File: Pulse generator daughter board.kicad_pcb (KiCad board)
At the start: 2 copper layers, 31 parts, among them U1 MAX31855KASA, U3 TC4427, U4 TC4427

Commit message: Progress on PCB 29.11.2024
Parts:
- removed R26: 10k, Resistor_SMD:R_0805_2012Metric_Pad1.20x1.40mm_HandSolder
- added C1: C, Capacitor_SMD:C_0805_2012Metric_Pad1.18x1.45mm_HandSolder, F.Cu at (107.5, 87.5)
- added C10: C, Capacitor_SMD:C_0805_2012Metric_Pad1.18x1.45mm_HandSolder, F.Cu at (44.7, 105.5)
- added C11: C, Capacitor_SMD:C_0805_2012Metric_Pad1.18x1.45mm_HandSolder, F.Cu at (44.7, 108.5)
- added C12: 100nF, Capacitor_SMD:C_0805_2012Metric_Pad1.18x1.45mm_HandSolder, F.Cu at (106.0, 120.0)
- added C13: 100nF, Capacitor_SMD:C_0805_2012Metric_Pad1.18x1.45mm_HandSolder, F.Cu at (107.5, 137.0)
- added C14: 100nF, Capacitor_SMD:C_0805_2012Metric_Pad1.18x1.45mm_HandSolder, F.Cu at (78.0, 115.0)
- added C15: 100nF, Capacitor_SMD:C_0805_2012Metric_Pad1.18x1.45mm_HandSolder, F.Cu at (93.5, 115.0)
- added C2: C, Capacitor_SMD:C_0805_2012Metric_Pad1.18x1.45mm_HandSolder, F.Cu at (80.5, 99.0)
- added C3: 10nF, Capacitor_SMD:C_0805_2012Metric_Pad1.18x1.45mm_HandSolder, F.Cu at (118.0, 135.0)
- added C4: C, Capacitor_SMD:C_0805_2012Metric_Pad1.18x1.45mm_HandSolder, F.Cu at (109.5, 113.0)
- added C5: 100nF, Capacitor_SMD:C_0805_2012Metric_Pad1.18x1.45mm_HandSolder, F.Cu at (118.0, 131.5)
- added C6: C, Capacitor_SMD:C_0805_2012Metric_Pad1.18x1.45mm_HandSolder, F.Cu at (109.5, 115.5)
- added C7: C, Capacitor_SMD:C_0805_2012Metric_Pad1.18x1.45mm_HandSolder, F.Cu at (39.8, 108.5)
- added C8: C, Capacitor_SMD:C_0805_2012Metric_Pad1.18x1.45mm_HandSolder, F.Cu at (44.7, 99.5)
- added C9: C, Capacitor_SMD:C_0805_2012Metric_Pad1.18x1.45mm_HandSolder, F.Cu at (94.0, 98.5)
- added J1: Vin1, Connector_Wire:SolderWire-0.5sqmm_1x01_D0.9mm_OD2.1mm, F.Cu at (77.0, 46.5)
- added J10: Vin2_GND, Connector_Wire:SolderWire-0.5sqmm_1x01_D0.9mm_OD2.1mm, F.Cu at (109.0, 51.5)
- added J11: CN8, Connector_PinHeader_2.54mm:PinHeader_2x08_P2.54mm_Vertical, F.Cu at (68.0, 47.8)
- added J12: CN9, Connector_PinHeader_2.54mm:PinHeader_2x15_P2.54mm_Vertical, F.Cu at (67.5, 82.1)
- added J13: CN7, Connector_PinHeader_2.54mm:PinHeader_2x10_P2.54mm_Vertical, F.Cu at (117.0, 47.3)
- added J14: CN10, Connector_PinHeader_2.54mm:PinHeader_2x17_P2.54mm_Vertical, F.Cu at (117.0, 77.2)
- added J15: CH1 output, Connector_Wire:SolderWire-0.5sqmm_1x01_D0.9mm_OD2.1mm, F.Cu at (66.5, 135.0)
- added J16: GND, Connector_Wire:SolderWire-0.5sqmm_1x01_D0.9mm_OD2.1mm, F.Cu at (66.5, 140.0)
- added J17: CH2 output, Connector_Wire:SolderWire-0.5sqmm_1x01_D0.9mm_OD2.1mm, F.Cu at (85.0, 135.0)
- added J18: GND, Connector_Wire:SolderWire-0.5sqmm_1x01_D0.9mm_OD2.1mm, F.Cu at (85.0, 140.0)
- added J2: Vin1_GND, Connector_Wire:SolderWire-0.5sqmm_1x01_D0.9mm_OD2.1mm, F.Cu at (77.0, 51.5)
- added J7: T+, Connector_Wire:SolderWire-0.5sqmm_1x01_D0.9mm_OD2.1mm, F.Cu at (120.0, 139.5)
- added J8: T-, Connector_Wire:SolderWire-0.5sqmm_1x01_D0.9mm_OD2.1mm, F.Cu at (114.0, 139.5)
- added J9: Vin2, Connector_Wire:SolderWire-0.5sqmm_1x01_D0.9mm_OD2.1mm, F.Cu at (109.0, 46.5)
- added U1: RYK-053.3SH, Rafal:RYK-053.3SH, F.Cu at (109.8, 93.5)
- added U3: ADUM1402, Package_SO:SOIC-16W_7.5x10.3mm_P1.27mm, F.Cu at (109.0, 128.0)
- moved R16 84.6 mm to (83.5, 115.0), turned to 180 degrees
- moved R17 71.1 mm to (99.0, 115.0), turned to 180 degrees
- moved D1 64.0 mm to (85.5, 47.5)
- moved R14 58.1 mm to (93.4, 71.5)
- moved R15 58.1 mm to (93.4, 74.4)
- moved D8 55.5 mm to (85.0, 126.5), turned to 90 degrees
- moved D7 49.2 mm to (66.5, 126.5), turned to 90 degrees
- moved D6 47.6 mm to (100.5, 47.5)
- moved U2 38.8 mm to (119.0, 125.5), turned to 90 degrees
- moved R22 38.6 mm to (73.0, 126.0), turned to 90 degrees
- moved R25 36.6 mm to (97.3, 135.9)
- moved R21 35.9 mm to (97.3, 126.0)
- moved R24 35.5 mm to (91.5, 135.9)
- moved R20 34.7 mm to (91.5, 126.0)
- moved U5 34.1 mm to (99.8, 103.7)
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- renumbered D6 to D1, D8 to D6, D1 to D8, R20 to R19, R22 to R20, R23 to R21, R19 to R22, R21 to R23, U1 to U2, U3 to U4, U4 to U5
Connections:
- net Net-(J19-Pin_1) renamed /PWM1 _CH1
- net Net-(J20-Pin_1) renamed /PWM1 _CH2
- R11 pad 2: unconnected-(R11-Pad2) -> GND
- R12 pad 2: Net-(J11-Pin_1) -> /ADC1
- R13 pad 2: Net-(J13-Pin_1) -> /ADC2
- R9 pad 2: unconnected-(R9-Pad2) -> GND
- U2 pad 4: +3V3_TC -> Net-(U1-+Vout)
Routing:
- net GND: track 0.00 -> 2.20 mm, vias 0 -> 1
- added copper zone on In1.Cu, net GND
- added copper zone on In2.Cu, net GND
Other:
- board outline added: 60 x 100 mm
- copper layers 2 -> 4
- board text added: "60x80"

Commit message: Connector position locked + some more progress
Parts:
- added D2: 20V, Diode_SMD:D_SOD-323F, F.Cu at (96.8, 73.7)
- added D3: 20V, Diode_SMD:D_SOD-323F, F.Cu at (96.8, 76.7)
- added D4: 20V, Diode_SMD:D_SOD-323F, F.Cu at (96.8, 79.6)
- added D9: 20V, Diode_SMD:D_SOD-323F, F.Cu at (96.8, 82.6)
- added J3: 3V3, Connector_Wire:SolderWire-0.5sqmm_1x01_D0.9mm_OD2.1mm, F.Cu at (93.8, 45.1)
- added J4: DVM1, Connector_Wire:SolderWire-0.5sqmm_1x01_D0.9mm_OD2.1mm, F.Cu at (93.8, 49.3)
- added J5: 3V3, Connector_Wire:SolderWire-0.5sqmm_1x01_D0.9mm_OD2.1mm, F.Cu at (93.8, 53.4)
- added J6: DVM1, Connector_Wire:SolderWire-0.5sqmm_1x01_D0.9mm_OD2.1mm, F.Cu at (93.8, 57.6)
- added R1: R, Resistor_SMD:R_0805_2012Metric_Pad1.20x1.40mm_HandSolder, F.Cu at (84.3, 74.1)
- added R2: R, Resistor_SMD:R_0805_2012Metric_Pad1.20x1.40mm_HandSolder, F.Cu at (84.3, 77.1)
- added U6: MAX31856, Package_SO:TSSOP-14_4.4x5mm_P0.65mm, F.Cu at (179.3, 125.1)
- moved R18 50.7 mm to (123.1, 128.4), turned to 180 degrees
- moved J11 46.8 mm to (113.8, 57.3)
- moved R19 46.4 mm to (123.2, 122.7), turned to 180 degrees
- moved J12 46.4 mm to (113.8, 80.2)
- moved R7 46.3 mm to (123.0, 66.4)
- moved R8 46.3 mm to (124.0, 72.4)
- moved U4 46.3 mm to (130.6, 103.3)
- moved C10 46.3 mm to (91.0, 105.1)
- moved C11 46.3 mm to (91.0, 108.1)
- moved C14 46.3 mm to (124.3, 114.6)
- moved C2 46.3 mm to (126.8, 98.6)
- moved C7 46.3 mm to (86.2, 108.1)
- moved C8 46.3 mm to (91.0, 99.1)
- moved R10 46.3 mm to (135.1, 59.1)
- moved R11 46.3 mm to (135.1, 62.1)
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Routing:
- net GND: vias 1 -> 0
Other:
- board size 60 x 100 mm -> 60 x 104.7 mm
- board text removed: "60x80"

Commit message: Positioning done
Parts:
- removed the J3 at (93.8, 45.1)
- removed the J5 at (93.8, 53.4)
- removed the U2 at (164.6, 131.3)
- added C18: 100nF, Capacitor_SMD:C_0805_2012Metric_Pad1.18x1.45mm_HandSolder, F.Cu at (139.5, 59.0)
- added C19: 100nF, Capacitor_SMD:C_0805_2012Metric_Pad1.18x1.45mm_HandSolder, F.Cu at (139.5, 68.2)
- added C4: 100nF, Capacitor_SMD:C_0805_2012Metric_Pad1.18x1.45mm_HandSolder, F.Cu at (180.7, 138.5)
- added C5: 10nF, Capacitor_SMD:C_0805_2012Metric_Pad1.18x1.45mm_HandSolder, F.Cu at (180.7, 141.5)
- added C7: 10nF, Capacitor_SMD:C_0805_2012Metric_Pad1.18x1.45mm_HandSolder, F.Cu at (180.7, 144.5)
- added D10: 20V, Diode_SMD:D_SOD-323F, F.Cu at (129.0, 86.7)
- added D9: 20V, Diode_SMD:D_SOD-323F, F.Cu at (142.2, 86.7)
- added J10: GND, Connector_Wire:SolderWire-0.5sqmm_1x01_D0.9mm_OD2.1mm, F.Cu at (102.0, 91.0)
- added J11: Power_on LED, Connector_Wire:SolderWire-0.5sqmm_1x01_D0.9mm_OD2.1mm, F.Cu at (113.0, 46.5)
- added J12: Power_on LED_ret, Connector_Wire:SolderWire-0.5sqmm_1x01_D0.9mm_OD2.1mm, F.Cu at (113.0, 51.5)
- added J21: GND, Connector_Wire:SolderWire-0.5sqmm_1x01_D0.9mm_OD2.1mm, F.Cu at (123.2, 84.2)
- added J22: GND, Connector_Wire:SolderWire-0.5sqmm_1x01_D0.9mm_OD2.1mm, F.Cu at (136.7, 84.2)
- added J23: Switch_1, Connector_Wire:SolderWire-0.5sqmm_1x01_D0.9mm_OD2.1mm, F.Cu at (123.2, 89.7)
- added J24: Switch_1, Connector_Wire:SolderWire-0.5sqmm_1x01_D0.9mm_OD2.1mm, F.Cu at (136.7, 89.7)
- added J8: GND, Connector_Wire:SolderWire-0.5sqmm_1x01_D0.9mm_OD2.1mm, F.Cu at (102.0, 78.0)
- added R1: R, Resistor_SMD:R_0805_2012Metric_Pad1.20x1.40mm_HandSolder, F.Cu at (180.6, 147.5)
- added R19: DNF, Resistor_SMD:R_0805_2012Metric_Pad1.20x1.40mm_HandSolder, F.Cu at (134.5, 54.5)
- added R2: R, Resistor_SMD:R_0805_2012Metric_Pad1.20x1.40mm_HandSolder, F.Cu at (180.6, 150.4)
- added R20: DNF, Resistor_SMD:R_0805_2012Metric_Pad1.20x1.40mm_HandSolder, F.Cu at (134.5, 63.7)
- added R23: DNF, Resistor_SMD:R_0805_2012Metric_Pad1.20x1.40mm_HandSolder, F.Cu at (135.5, 59.0)
- added R24: DNF, Resistor_SMD:R_0805_2012Metric_Pad1.20x1.40mm_HandSolder, F.Cu at (135.5, 68.2)
- added R33: 43R, Resistor_SMD:R_2512_6332Metric_Pad1.40x3.35mm_HandSolder, F.Cu at (142.7, 77.0)
- added R34: 43R, Resistor_SMD:R_2512_6332Metric_Pad1.40x3.35mm_HandSolder, F.Cu at (137.0, 77.0)
- added R35: 43R, Resistor_SMD:R_2512_6332Metric_Pad1.40x3.35mm_HandSolder, F.Cu at (129.2, 77.0)
- added R36: 43R, Resistor_SMD:R_2512_6332Metric_Pad1.40x3.35mm_HandSolder, F.Cu at (123.5, 77.0)
- added R5: 10k, Resistor_SMD:R_0805_2012Metric_Pad1.20x1.40mm_HandSolder, F.Cu at (124.7, 55.2)
- added TR1: RQ5H020TNTL, Rafal:SOT-346T, F.Cu at (145.0, 59.0)
- added TR2: RQ5H020TNTL, Rafal:SOT-346T, F.Cu at (145.0, 68.2)
- J3: renamed from J1; value Vin1 -> Vin1_PSU
- J5: renamed from J9; value Vin2 -> Vin2_PSU
- U3: value ADUM1402 -> ADuM1401xRW
- moved C12 59.0 mm to (105.7, 48.0), turned to 180 degrees
- moved C10 56.7 mm to (102.2, 53.7)
- moved R14 54.1 mm to (102.0, 104.9), turned to 180 degrees
- moved R13 53.7 mm to (107.0, 104.9), turned to 180 degrees
- moved R16 48.4 mm to (102.2, 109.6), turned to -90 degrees
- moved C2 47.0 mm to (124.6, 51.7), turned to 0 degrees
- moved C3 46.8 mm to (145.6, 51.9)
- moved R8 42.6 mm to (107.0, 100.6), turned to 180 degrees
- moved R9 40.2 mm to (102.0, 100.6), turned to 180 degrees
- moved R15 30.6 mm to (107.0, 53.0), turned to 90 degrees
- moved J9 29.4 mm to (102.0, 85.9), turned to -90 degrees
- moved R17 28.3 mm to (126.2, 96.0)
- moved R6 28.3 mm to (102.2, 62.7)
- moved R12 27.9 mm to (107.2, 57.7)
- moved R4 26.6 mm to (107.0, 91.1), turned to -90 degrees
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- renumbered C7 to C10, C8 to C11, C10 to C12, C11 to C13, C12 to C14, C13 to C15, C14 to C16, C15 to C17, C9 to C3, C4 to C6, C6 to C8, C5 to C9, D6 to D2, D2 to D3, D9 to D4, D3 to D5, D4 to D6, J7 to J1, J11 to J13, J12 to J14, J13 to J15, J14 to J16, J15 to J17, J16 to J18, J17 to J19, J8 to J2, J18 to J20, J2 to J4, J10 to J6, J4 to J7, J6 to J9, R3 to R10, R8 to R11, R9 to R12, R10 to R13, R11 to R14, R12 to R15, R13 to R16, R14 to R17, R15 to R18, R16 to R21, R17 to R22, R18 to R25, R19 to R26, R20 to R27, R21 to R28, R22 to R29, R1 to R3, R23 to R30, R24 to R31, R25 to R32, R2 to R4, R4 to R6, R5 to R7, R6 to R8, R7 to R9, U6 to U2
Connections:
- C10 pad 1: Net-(J3-Pin_1) -> +3V3
- C11 pad 1: Net-(J5-Pin_1) -> +3V3
- J1 pad 1: Net-(J7-Pin_1) -> Net-(J1-Pin_1)
- J13 pad 11: unconnected-(J11-Pin_11-Pad11) -> GND
- J13 pad 13: unconnected-(J11-Pin_13-Pad13) -> GND
- J13 pad 15: unconnected-(J11-Pin_15-Pad15) -> Vin1
- J13 pad 7: unconnected-(J11-Pin_7-Pad7) -> +3V3
- J14 pad 12: unconnected-(J12-Pin_12-Pad12) -> GND
- J14 pad 23: unconnected-(J12-Pin_23-Pad23) -> GND
- J15 pad 14: unconnected-(J13-Pin_14-Pad14) (its old number) -> /SPI_MOSI
- J15 pad 15: Net-(J13-Pin_15) -> /SPI1_SCLK
- J15 pad 19: Net-(J13-Pin_19) -> /SPI1_MISO
- J15 pad 2: Net-(J13-Pin_2) -> /SPI1_CS
- J15 pad 8: unconnected-(J13-Pin_8-Pad8) (its old number) -> GND
- J16 pad 14: unconnected-(J14-Pin_14-Pad14) (its old number) -> /Switch_1
- J16 pad 16: unconnected-(J14-Pin_16-Pad16) (its old number) -> /Switch_2
- J16 pad 17: unconnected-(J14-Pin_17-Pad17) (its old number) -> GND
- J16 pad 22: unconnected-(J14-Pin_22-Pad22) (its old number) -> GND
- J16 pad 27: unconnected-(J14-Pin_27-Pad27) (its old number) -> GND
- J16 pad 5: unconnected-(J14-Pin_5-Pad5) (its old number) -> GND
- J2 pad 1: Net-(J8-Pin_1) -> Net-(J2-Pin_1)
- J7 pad 1: Net-(J4-Pin_1) -> Net-(J7-Pin_1)
- R11 pad 1: Net-(J3-Pin_1) -> +3V3
- R13 pad 1: Net-(J5-Pin_1) -> +3V3
- R3 pad 1: Net-(J4-Pin_1) -> Net-(J7-Pin_1)
- U2 pad 1: unconnected-(U6-AGND-Pad1) -> OV_TC
- U2 pad 10: unconnected-(U6-SCK-Pad10) -> Net-(U2-SCK)
- U2 pad 11: unconnected-(U6-SDO-Pad11) -> Net-(U2-SDO)
- U2 pad 12: unconnected-(U6-SDI-Pad12) -> Net-(U2-SDI)
- U2 pad 14: unconnected-(U6-DGND-Pad14) -> OV_TC
- U2 pad 2: unconnected-(U6-BIAS-Pad2) -> Net-(J2-Pin_1)
- U2 pad 3: unconnected-(U6-T--Pad3) -> Net-(U2-T-)
- U2 pad 4: unconnected-(U6-T+-Pad4) -> Net-(U2-T+)
- U2 pad 5: unconnected-(U6-AVDD-Pad5) -> Net-(U1-+Vout)
- U2 pad 8: unconnected-(U6-DVDD-Pad8) -> Net-(U1-+Vout)
- U2 pad 9: unconnected-(U6-~{CS}-Pad9) -> Net-(U2-~{CS})
- U3 pad 1: Net-(U1-+Vout) -> +3V3
- U3 pad 10: GND -> Net-(U1-+Vout)
- U3 pad 11: Net-(J13-Pin_15) -> Net-(U2-SDO)
- U3 pad 12: Net-(J13-Pin_2) -> Net-(U2-~{CS})
- U3 pad 13: unconnected-(U3-Vob-Pad13) -> Net-(U2-SCK)
- U3 pad 14: Net-(J13-Pin_19) -> Net-(U2-SDI)
- U3 pad 15: GND -> OV_TC
- U3 pad 16: +3V3 -> Net-(U1-+Vout)
- U3 pad 2: OV_TC -> GND
- U3 pad 3: Net-(U2-SO) -> /SPI_MOSI
- U3 pad 4: OV_TC -> /SPI1_SCLK
- U3 pad 5: Net-(U2-~{CS}) -> /SPI1_CS
- U3 pad 6: Net-(U2-SCK) -> /SPI1_MISO
- U3 pad 7: OV_TC -> +3V3
- U3 pad 8: OV_TC -> GND
- U3 pad 9: GND -> OV_TC
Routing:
- net GND: track 2.20 -> 0.00 mm
- removed copper zone on In1.Cu, net GND
- removed copper zone on In2.Cu, net GND
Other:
- board size 60 x 104.7 mm -> 72.2 x 104.7 mm

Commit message: LAyout finished
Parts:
- removed the C3 at (161.8, 138.6)
- added C20: EMI cap, Capacitor_SMD:C_0805_2012Metric_Pad1.18x1.45mm_HandSolder, F.Cu at (143.2, 142.0)
- moved C5 27.1 mm to (154.5, 134.7), turned to 180 degrees
- moved R2 26.2 mm to (157.5, 138.2), turned to 180 degrees
- moved R19 24.2 mm to (151.5, 71.7), turned to 0 degrees
- moved C4 22.0 mm to (159.7, 131.7), turned to 180 degrees
- moved U2 21.6 mm to (157.7, 124.7)
- moved R1 19.5 mm to (163.5, 138.2)
- moved R24 18.2 mm to (150.5, 58.0), turned to 90 degrees
- moved C7 18.1 mm to (165.5, 134.7)
- moved C15 17.4 mm to (137.4, 125.0), turned to 90 degrees
- moved R23 17.1 mm to (150.5, 67.2), turned to 90 degrees
- moved R20 17.0 mm to (151.5, 62.5), turned to 0 degrees
- moved C9 12.4 mm to (162.7, 122.7), turned to 0 degrees
- moved C19 12.4 mm to (146.5, 58.0), turned to 90 degrees
- moved TR2 11.0 mm to (141.0, 58.0), turned to 90 degrees
- moved C18 10.8 mm to (146.5, 67.2), turned to 90 degrees
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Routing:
- net +3V3: track 0.00 -> 183.1 mm, vias 0 -> 7
- net /SPI1_CS: track 0.00 -> 115.0 mm, vias 0 -> 2
- net Vin1: track 0.00 -> 97.2 mm, vias 0 -> 3
- net /SPI_MOSI: track 0.00 -> 85.3 mm, vias 0 -> 2
- net Vin2: track 0.00 -> 83.9 mm, vias 0 -> 4
- net /SPI1_SCLK: track 0.00 -> 81.2 mm, vias 0 -> 2
- net /SPI1_MISO: track 0.00 -> 78.6 mm, vias 0 -> 1
- net GND: track 0.00 -> 68.9 mm, vias 0 -> 39
- net /PWM1 _CH1: track 0.00 -> 65.0 mm, vias 0 -> 1
- net /+5V: track 0.00 -> 58.4 mm, vias 0 -> 1
- net Net-(U1-+Vout): track 0.00 -> 45.4 mm, vias 0 -> 2
- net Net-(U5-OUT_A): track 0.00 -> 39.3 mm
- net /ADC1: track 0.00 -> 37.7 mm
- net /Switch_2: track 0.00 -> 37.6 mm
- net OV_TC: track 0.00 -> 37.4 mm, vias 0 -> 9
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- added copper zone on In1.Cu, net GND
- added copper zone on In2.Cu, net GND
- added copper zone on In1.Cu, net OV_TC
- added copper zone on In2.Cu, net OV_TC
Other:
- board text added: "C20 is EMI suppression cap"

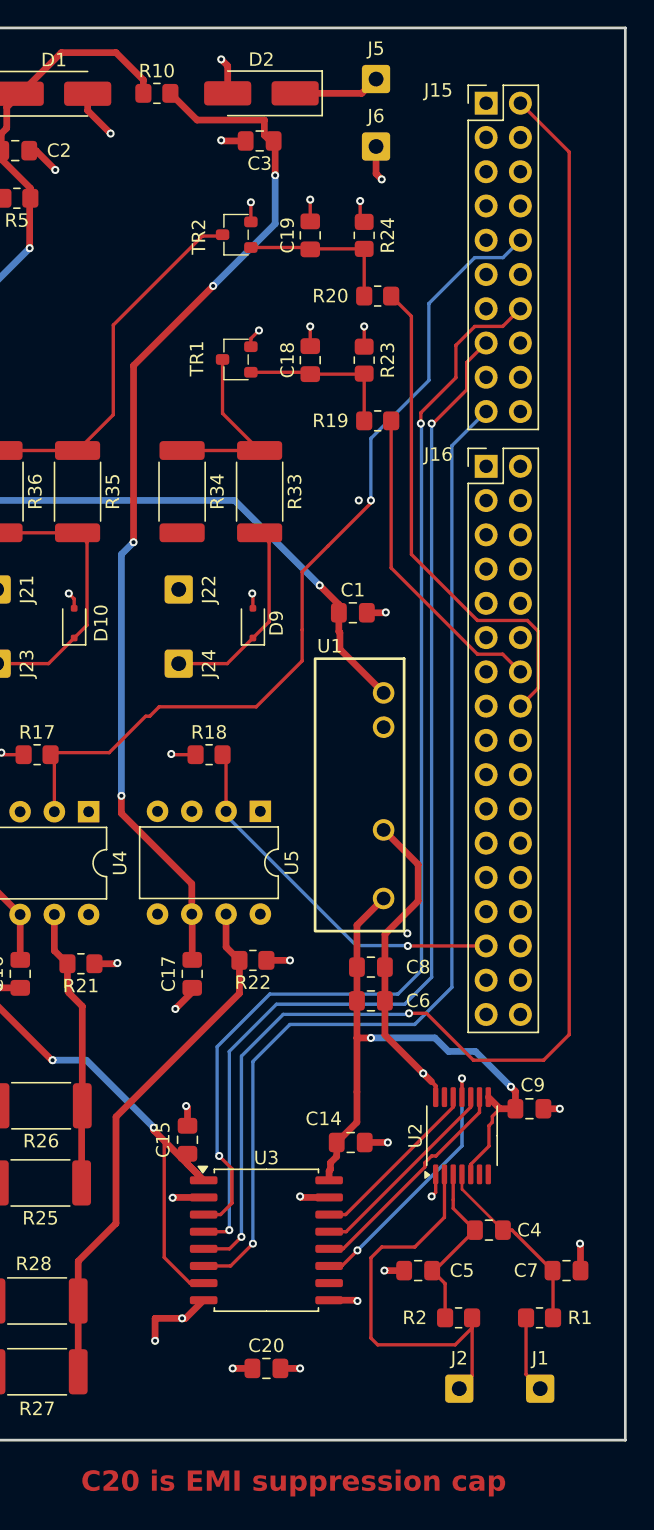
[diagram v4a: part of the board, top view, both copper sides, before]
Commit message: LAyout finished + small corrections
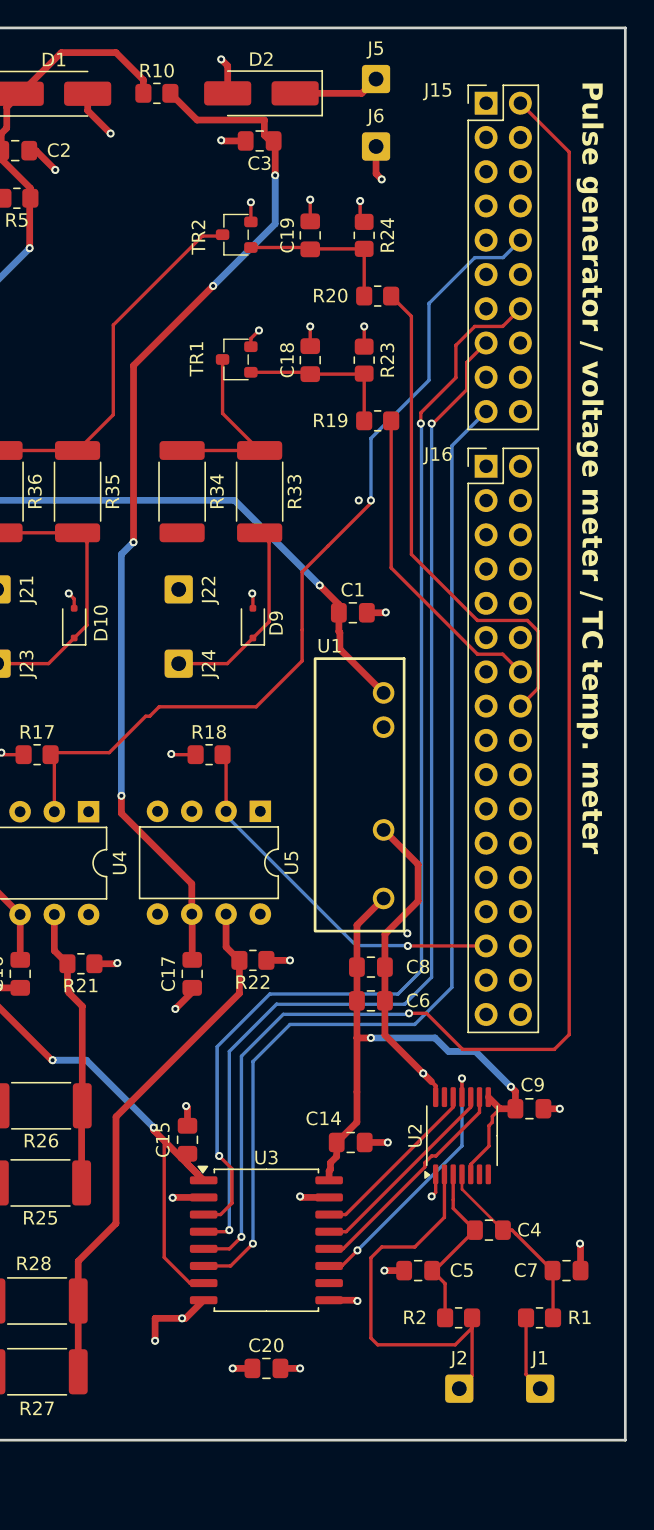
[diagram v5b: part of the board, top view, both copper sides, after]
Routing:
- net /SPI1_CS: track 115.0 -> 114.3 mm
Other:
- board text added: "Pulse generator / voltage meter / TC temp. meter"
- board text removed: "C20 is EMI suppression cap"
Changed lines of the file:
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@@
 		(layer "Edge.Cuts")
 	)
-	(gr_text "C20 is EMI suppression cap"
-		(at 129.46 151.22 0)
-		(layer "F.Cu")
+	(gr_text "Pulse generator / voltage meter / TC temp. meter"
+		(at 166.46 46.52 270)
+		(layer "F.SilkS")
 		(effects
 			(font
@@
 	)
 	(segment
-		(start 163.76 119.12)
-		(end 165.66 117.22)
-		(width 0.25)
-		(layer "F.Cu")
-		(net 63)
-	)
-	(segment
-		(start 165.66 117.22)
-		(end 165.66 51.79)
+		(start 141.36 132.22)
+		(end 140.475 133.105)
 		(width 0.25)
 		(layer "F.Cu")
@@
 	)
 	(segment
-		(start 141.36 132.22)
-		(end 140.475 133.105)
+		(start 153.785 115.645)
+		(end 155.085 115.645)
 		(width 0.25)
 		(layer "F.Cu")
@@
 	(segment
 		(start 155.085 115.645)
-		(end 158.56 119.12)
+		(end 157.76 118.32)
 		(width 0.25)
 		(layer "F.Cu")
@@
 	)
 	(segment
-		(start 153.785 115.645)
-		(end 155.085 115.645)
+		(start 164.56 118.32)
+		(end 165.66 117.22)
 		(width 0.25)
 		(layer "F.Cu")
@@
 	)
 	(segment
-		(start 158.56 119.12)
-		(end 163.76 119.12)
+		(start 157.76 118.32)
+		(end 164.56 118.32)
+		(width 0.25)
+		(layer "F.Cu")
+		(net 63)
+	)
+	(segment
+		(start 165.66 117.22)
+		(end 165.66 51.79)
 		(width 0.25)
 		(layer "F.Cu")

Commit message: 4 unconnected pads on PCB fixed
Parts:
- C2, C3: value C -> 10uF
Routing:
- net Net-(U1-+Vout): track 45.4 -> 58.2 mm
- net Net-(D9-K): track 14.9 -> 20.6 mm
- net Net-(D5-K): track 4.71 -> 9.00 mm
- net Vin2: track 83.9 -> 87.0 mm
